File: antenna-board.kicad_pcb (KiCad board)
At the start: 2 copper layers, 42.4 x 42.4 mm, 2 parts, among them J1 Conn_01x01, U1 U.FLport

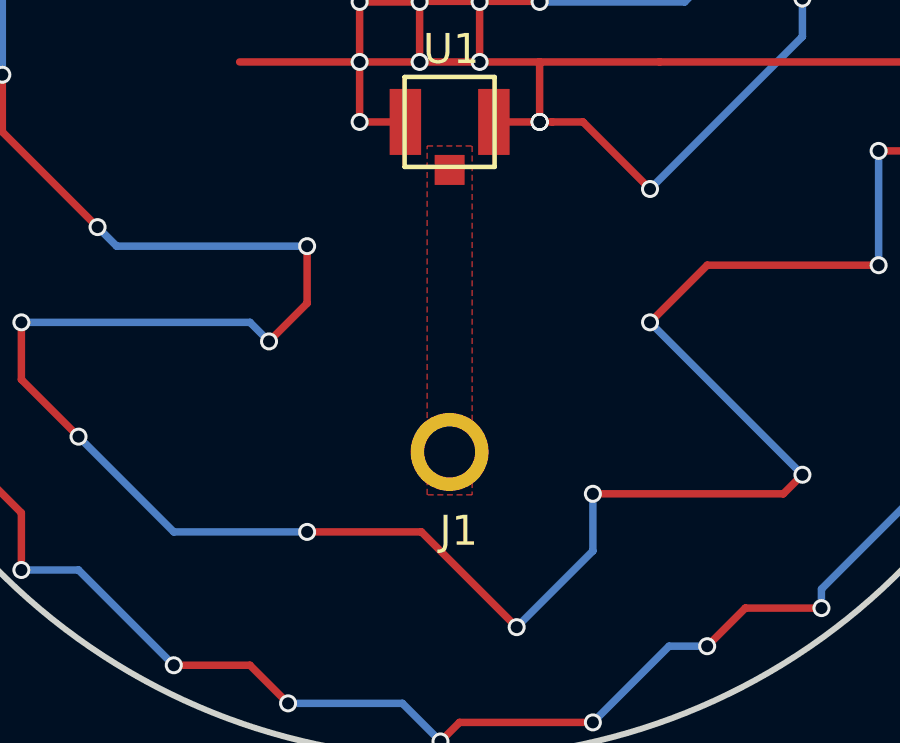
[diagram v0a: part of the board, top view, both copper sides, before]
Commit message: fixed bottom pad so its aligned, added via sheilding around data line.
Harrison helped. I derped a bit.
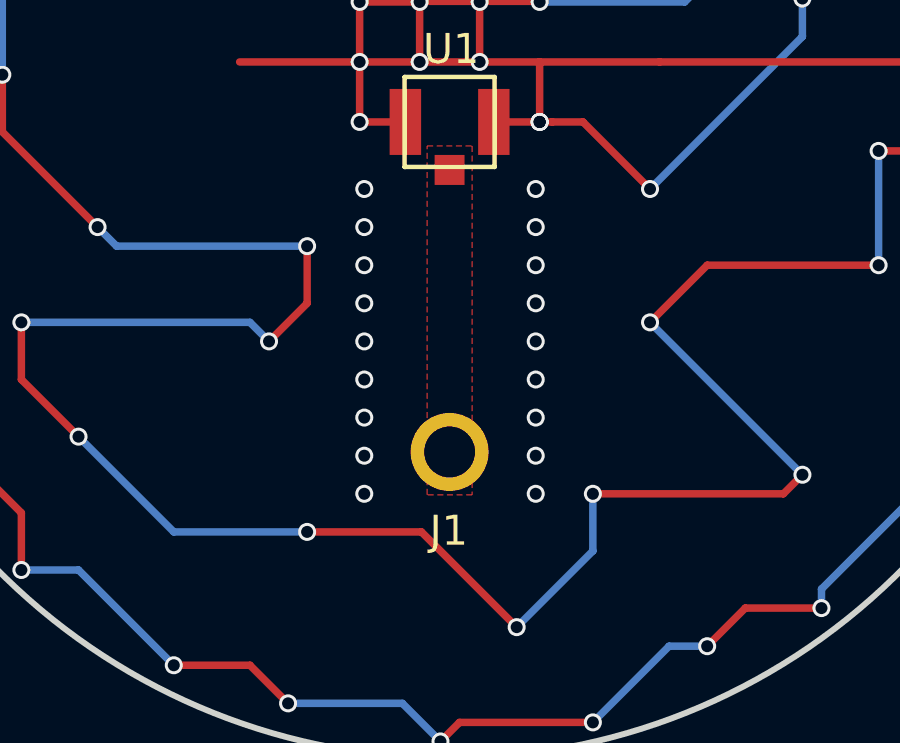
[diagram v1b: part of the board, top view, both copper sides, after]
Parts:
- moved J1 0.33 mm to (100.0, 111.8)
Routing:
- net (no net): vias 0 -> 18
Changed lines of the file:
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@@
     (thickness 1.6)
     (drawings 2)
-    (tracks 195)
+    (tracks 212)
     (zones 0)
     (modules 2)
@@
   )
   (module HelicalAntennaBoard:antenna_connector (layer F.Cu)
-    (at 100.33 111.76)
+    (at 100 111.76)
     (fp_text reference J1 (at -0.03 1.87) (layer F.SilkS)
       (effects (font (size 1 1) (thickness 0.15)))
@@
       (effects (font (size 1 1) (thickness 0.15)))
     )
-    (pad 1 thru_hole circle (at -0.33 -0.76) (size 2.6 2.6) (drill 1.7) (layers *.Cu *.Mask)
+    (pad 1 thru_hole circle (at 0 -0.76) (size 2.6 2.6) (drill 1.7) (layers *.Cu *.Mask)
       (net 1 DATA))
   )
@@
   )
   (gr_circle (center 100 100) (end 115 115) (layer Edge.Cuts) (width 0.2))
-  (segment (start 100 111.43) (end 100.33 111.76) (width 0.25) (layer F.Cu) (net 1))
+  (via (at 97.155 112.395) (size 0.6) (drill 0.4) (layers F.Cu B.Cu) (net 0))
+  (via (at 97.155 111.125) (size 0.6) (drill 0.4) (layers F.Cu B.Cu) (net 0))
+  (via (at 97.155 109.855) (size 0.6) (drill 0.4) (layers F.Cu B.Cu) (net 0))
+  (via (at 97.155 108.585) (size 0.6) (drill 0.4) (layers F.Cu B.Cu) (net 0))
+  (via (at 97.155 107.315) (size 0.6) (drill 0.4) (layers F.Cu B.Cu) (net 0))
+  (via (at 97.155 106.045) (size 0.6) (drill 0.4) (layers F.Cu B.Cu) (net 0))
+  (via (at 97.155 104.775) (size 0.6) (drill 0.4) (layers F.Cu B.Cu) (net 0))
+  (via (at 97.155 103.505) (size 0.6) (drill 0.4) (layers F.Cu B.Cu) (net 0))
+  (via (at 97.155 102.235) (size 0.6) (drill 0.4) (layers F.Cu B.Cu) (net 0))
+  (via (at 102.87 112.395) (size 0.6) (drill 0.4) (layers F.Cu B.Cu) (net 0))
+  (via (at 102.87 111.125) (size 0.6) (drill 0.4) (layers F.Cu B.Cu) (net 0))
+  (via (at 102.87 109.855) (size 0.6) (drill 0.4) (layers F.Cu B.Cu) (net 0))
+  (via (at 102.87 108.585) (size 0.6) (drill 0.4) (layers F.Cu B.Cu) (net 0))
+  (via (at 102.87 107.315) (size 0.6) (drill 0.4) (layers F.Cu B.Cu) (net 0))
+  (via (at 102.87 106.045) (size 0.6) (drill 0.4) (layers F.Cu B.Cu) (net 0))
+  (via (at 102.87 104.775) (size 0.6) (drill 0.4) (layers F.Cu B.Cu) (net 0))
+  (via (at 102.87 103.505) (size 0.6) (drill 0.4) (layers F.Cu B.Cu) (net 0))
+  (via (at 102.87 102.235) (size 0.6) (drill 0.4) (layers F.Cu B.Cu) (net 0))
   (segment (start 93 98) (end 103 98) (width 0.25) (layer F.Cu) (net 2))
   (segment (start 107 98) (end 117.475 98) (width 0.25) (layer F.Cu) (net 2))
@@
     )
   )
-  (zone (net 0) (net_name "") (layer F.Cu) (hatch full 0.508)
+  (zone (net 1) (net_name DATA) (layer F.Cu) (hatch full 0.508)
+    (priority 11)
     (connect_pads yes (clearance 0.2))
     (min_thickness 1.2)
-    (keepout (tracks not_allowed) (vias not_allowed) (copperpour not_allowed))
     (fill yes (arc_segments 16) (thermal_gap 0.508) (thermal_bridge_width 0.508))
     (polygon
       (pts
-        (xy 100.965 101.6) (xy 102.235 101.6) (xy 102.22 109.7) (xy 100.95 109.7)
+        (xy 100.75 100.8) (xy 100.75 112.43) (xy 99.25 112.43) (xy 99.25 100.8)
       )
     )
@@
     )
   )
-  (zone (net 1) (net_name DATA) (layer F.Cu) (hatch full 0.508)
-    (priority 11)
+  (zone (net 0) (net_name "") (layer F.Cu) (hatch full 0.508)
     (connect_pads yes (clearance 0.2))
     (min_thickness 1.2)
-    (fill yes (arc_segments 16) (thermal_gap 0.508) (thermal_bridge_width 0.508))
-    (polygon
-      (pts
-        (xy 100.75 100.8) (xy 100.75 112.43) (xy 99.25 112.43) (xy 99.25 100.8)
-      )
-    )
+    (keepout (tracks not_allowed) (vias not_allowed) (copperpour not_allowed))
+    (fill (arc_segments 16) (thermal_gap 0.508) (thermal_bridge_width 0.508))
+    (polygon
+      (pts
+        (xy 100.965 101.6) (xy 102.235 101.6) (xy 102.22 109.7) (xy 100.95 109.7)
+      )
+    )

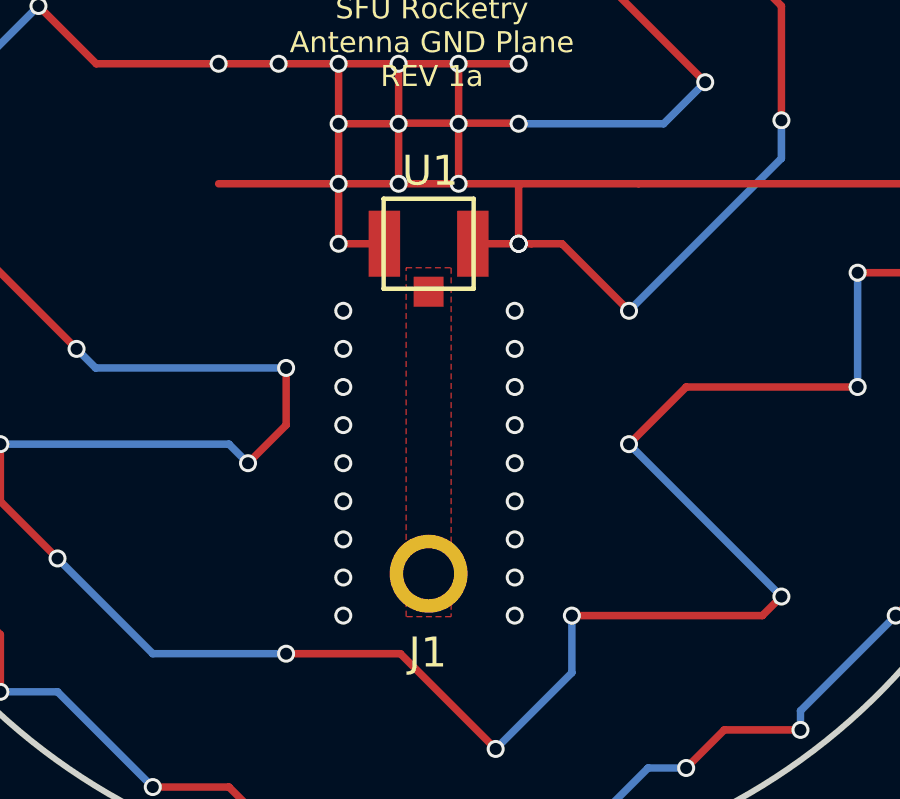
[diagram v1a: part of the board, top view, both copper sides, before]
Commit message: connected shielding vias and fixed area around data pad
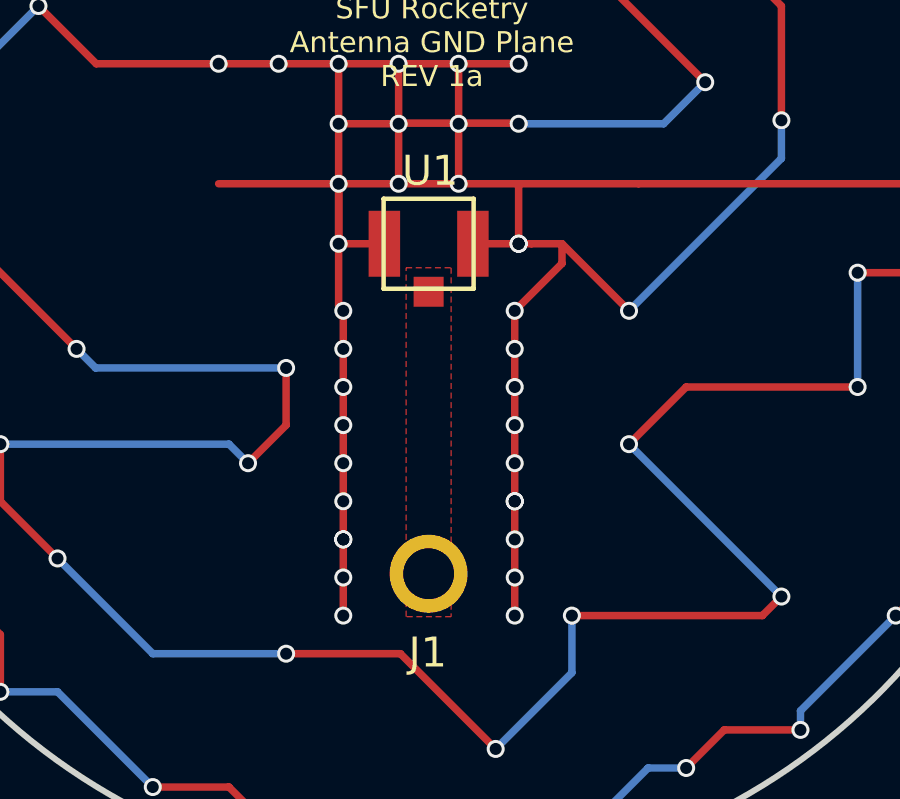
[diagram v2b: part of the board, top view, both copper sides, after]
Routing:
- net GNDREF: track 365.4 -> 393.1 mm, vias 65 -> 85
- net (no net): vias 18 -> 0
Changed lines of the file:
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@@
     (thickness 1.6)
     (drawings 2)
-    (tracks 212)
+    (tracks 235)
     (zones 0)
     (modules 2)
@@
   )
   (gr_circle (center 100 100) (end 115 115) (layer Edge.Cuts) (width 0.2))
-  (via (at 97.155 112.395) (size 0.6) (drill 0.4) (layers F.Cu B.Cu) (net 0))
-  (via (at 97.155 111.125) (size 0.6) (drill 0.4) (layers F.Cu B.Cu) (net 0))
-  (via (at 97.155 109.855) (size 0.6) (drill 0.4) (layers F.Cu B.Cu) (net 0))
-  (via (at 97.155 108.585) (size 0.6) (drill 0.4) (layers F.Cu B.Cu) (net 0))
-  (via (at 97.155 107.315) (size 0.6) (drill 0.4) (layers F.Cu B.Cu) (net 0))
-  (via (at 97.155 106.045) (size 0.6) (drill 0.4) (layers F.Cu B.Cu) (net 0))
-  (via (at 97.155 104.775) (size 0.6) (drill 0.4) (layers F.Cu B.Cu) (net 0))
-  (via (at 97.155 103.505) (size 0.6) (drill 0.4) (layers F.Cu B.Cu) (net 0))
-  (via (at 97.155 102.235) (size 0.6) (drill 0.4) (layers F.Cu B.Cu) (net 0))
-  (via (at 102.87 112.395) (size 0.6) (drill 0.4) (layers F.Cu B.Cu) (net 0))
-  (via (at 102.87 111.125) (size 0.6) (drill 0.4) (layers F.Cu B.Cu) (net 0))
-  (via (at 102.87 109.855) (size 0.6) (drill 0.4) (layers F.Cu B.Cu) (net 0))
-  (via (at 102.87 108.585) (size 0.6) (drill 0.4) (layers F.Cu B.Cu) (net 0))
-  (via (at 102.87 107.315) (size 0.6) (drill 0.4) (layers F.Cu B.Cu) (net 0))
-  (via (at 102.87 106.045) (size 0.6) (drill 0.4) (layers F.Cu B.Cu) (net 0))
-  (via (at 102.87 104.775) (size 0.6) (drill 0.4) (layers F.Cu B.Cu) (net 0))
-  (via (at 102.87 103.505) (size 0.6) (drill 0.4) (layers F.Cu B.Cu) (net 0))
-  (via (at 102.87 102.235) (size 0.6) (drill 0.4) (layers F.Cu B.Cu) (net 0))
+  (segment (start 104.445 100) (end 104.445 100.66) (width 0.25) (layer F.Cu) (net 2))
+  (segment (start 104.445 100.66) (end 102.87 102.235) (width 0.25) (layer F.Cu) (net 2))
+  (via (at 97.155 112.395) (size 0.6) (drill 0.4) (layers F.Cu B.Cu) (net 2))
+  (segment (start 97.155 111.125) (end 97.155 112.395) (width 0.25) (layer F.Cu) (net 2))
+  (via (at 97.155 111.125) (size 0.6) (drill 0.4) (layers F.Cu B.Cu) (net 2))
+  (segment (start 97.155 109.855) (end 97.155 111.125) (width 0.25) (layer F.Cu) (net 2))
+  (via (at 97.155 109.855) (size 0.6) (drill 0.4) (layers F.Cu B.Cu) (net 2))
+  (segment (start 97.155 108.585) (end 97.155 109.855) (width 0.25) (layer F.Cu) (net 2))
+  (via (at 97.155 109.855) (size 0.6) (drill 0.4) (layers F.Cu B.Cu) (net 2))
+  (via (at 97.155 108.585) (size 0.6) (drill 0.4) (layers F.Cu B.Cu) (net 2))
+  (segment (start 97.155 107.315) (end 97.155 108.585) (width 0.25) (layer F.Cu) (net 2))
+  (via (at 97.155 107.315) (size 0.6) (drill 0.4) (layers F.Cu B.Cu) (net 2))
+  (segment (start 97.155 106.045) (end 97.155 107.315) (width 0.25) (layer F.Cu) (net 2))
+  (via (at 97.155 106.045) (size 0.6) (drill 0.4) (layers F.Cu B.Cu) (net 2))
+  (segment (start 97.155 104.775) (end 97.155 106.045) (width 0.25) (layer F.Cu) (net 2))
+  (via (at 97.155 104.775) (size 0.6) (drill 0.4) (layers F.Cu B.Cu) (net 2))
+  (segment (start 97.155 103.505) (end 97.155 104.775) (width 0.25) (layer F.Cu) (net 2))
+  (via (at 97.155 103.505) (size 0.6) (drill 0.4) (layers F.Cu B.Cu) (net 2))
+  (segment (start 97.155 102.235) (end 97.155 103.505) (width 0.25) (layer F.Cu) (net 2))
+  (segment (start 97 98) (end 97 102.08) (width 0.25) (layer F.Cu) (net 2))
+  (segment (start 97 102.08) (end 97.155 102.235) (width 0.25) (layer F.Cu) (net 2))
+  (via (at 97.155 102.235) (size 0.6) (drill 0.4) (layers F.Cu B.Cu) (net 2))
+  (via (at 102.87 112.395) (size 0.6) (drill 0.4) (layers F.Cu B.Cu) (net 2))
+  (segment (start 102.87 111.125) (end 102.87 112.395) (width 0.25) (layer F.Cu) (net 2))
+  (via (at 102.87 111.125) (size 0.6) (drill 0.4) (layers F.Cu B.Cu) (net 2))
+  (segment (start 102.87 109.855) (end 102.87 111.125) (width 0.25) (layer F.Cu) (net 2))
+  (via (at 102.87 109.855) (size 0.6) (drill 0.4) (layers F.Cu B.Cu) (net 2))
+  (segment (start 102.87 108.585) (end 102.87 109.855) (width 0.25) (layer F.Cu) (net 2))
+  (via (at 102.87 108.585) (size 0.6) (drill 0.4) (layers F.Cu B.Cu) (net 2))
+  (segment (start 102.87 107.315) (end 102.87 108.585) (width 0.25) (layer F.Cu) (net 2))
+  (via (at 102.87 108.585) (size 0.6) (drill 0.4) (layers F.Cu B.Cu) (net 2))
+  (via (at 102.87 107.315) (size 0.6) (drill 0.4) (layers F.Cu B.Cu) (net 2))
+  (segment (start 102.87 106.045) (end 102.87 107.315) (width 0.25) (layer F.Cu) (net 2))
+  (via (at 102.87 106.045) (size 0.6) (drill 0.4) (layers F.Cu B.Cu) (net 2))
+  (segment (start 102.87 104.775) (end 102.87 106.045) (width 0.25) (layer F.Cu) (net 2))
+  (segment (start 102.87 103.505) (end 102.87 104.775) (width 0.25) (layer F.Cu) (net 2))
+  (via (at 102.87 104.775) (size 0.6) (drill 0.4) (layers F.Cu B.Cu) (net 2))
+  (via (at 102.87 103.505) (size 0.6) (drill 0.4) (layers F.Cu B.Cu) (net 2))
+  (segment (start 102.87 102.235) (end 102.87 103.505) (width 0.25) (layer F.Cu) (net 2))
+  (segment (start 103 102.105) (end 102.87 102.235) (width 0.25) (layer F.Cu) (net 2))
+  (via (at 102.87 102.235) (size 0.6) (drill 0.4) (layers F.Cu B.Cu) (net 2))
   (segment (start 93 98) (end 103 98) (width 0.25) (layer F.Cu) (net 2))
   (segment (start 107 98) (end 117.475 98) (width 0.25) (layer F.Cu) (net 2))
@@
     (min_thickness 1.2)
     (keepout (tracks not_allowed) (vias not_allowed) (copperpour not_allowed))
-    (fill (arc_segments 16) (thermal_gap 0.508) (thermal_bridge_width 0.508))
+    (fill yes (arc_segments 16) (thermal_gap 0.508) (thermal_bridge_width 0.508))
     (polygon
       (pts
-        (xy 97.79 101.670252) (xy 99.06 101.670252) (xy 99.05 109.7) (xy 97.79 109.7)
+        (xy 97.79 101.670252) (xy 99.06 101.670252) (xy 99.0346 112.5982) (xy 97.7746 112.5982)
       )
     )
@@
     (polygon
       (pts
-        (xy 100.965 101.6) (xy 102.235 101.6) (xy 102.22 109.7) (xy 100.95 109.7)
+        (xy 100.965 101.6) (xy 102.235 101.6) (xy 102.235 112.6236) (xy 100.965 112.6236)
       )
     )

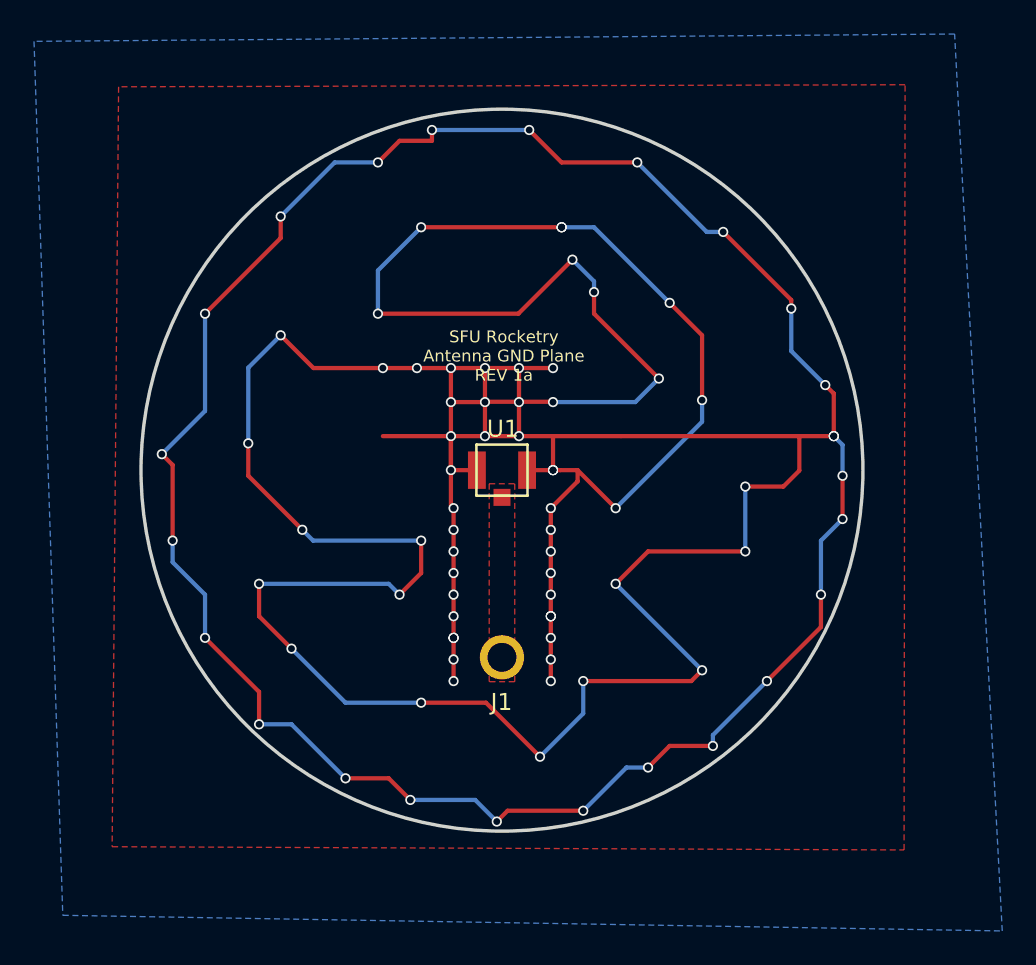
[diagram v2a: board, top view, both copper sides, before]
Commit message: fixed up some via tracks that were too close to the edge
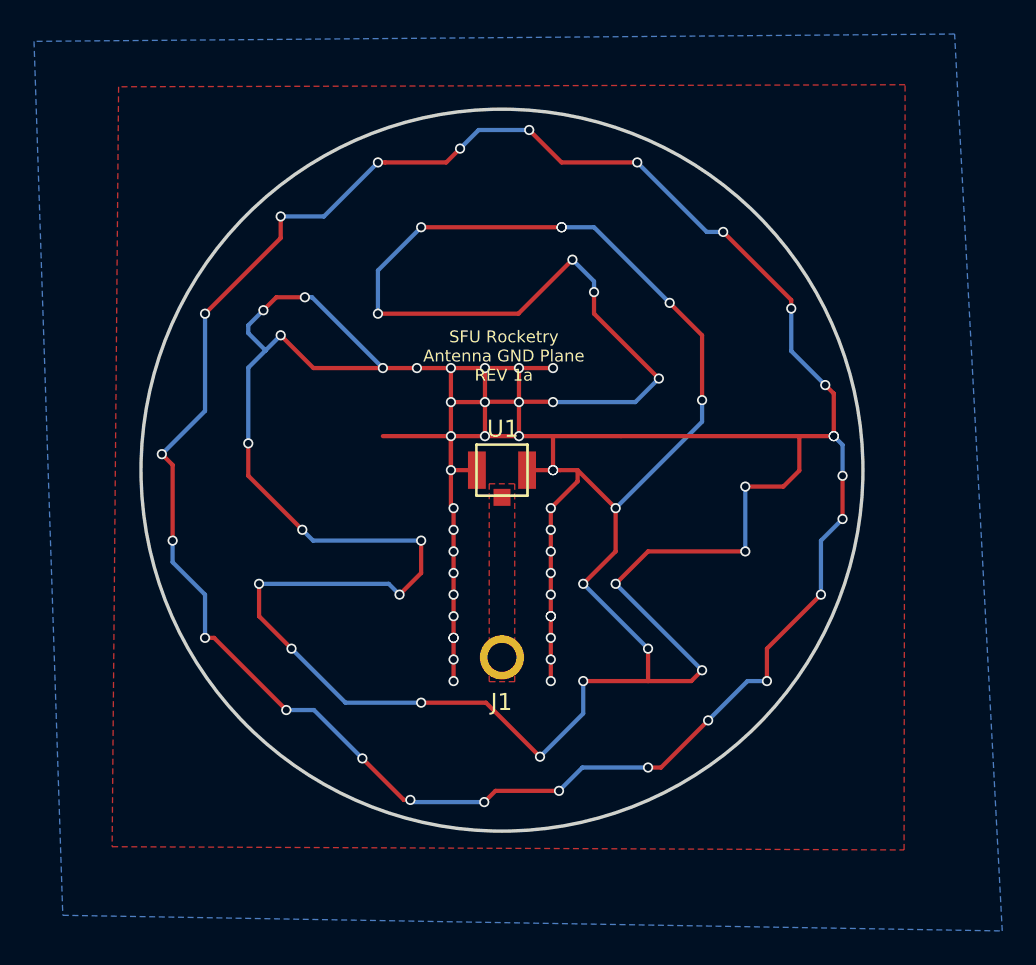
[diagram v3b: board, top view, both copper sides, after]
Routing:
- net GNDREF: track 393.1 -> 415.0 mm, vias 85 -> 89
